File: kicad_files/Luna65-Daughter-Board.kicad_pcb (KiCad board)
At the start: 2 copper layers, 25.1 x 25.1 mm, 38 parts, among them J1 TYPE-C-31-M12, J2 Molex Power, J3 JSTPH, Q1 MMUN2133LT1G, U1 MCP73831, U2 USBLC6-2SC6, U3 AP2112, U4 APX803L, U5 TPS61032RSAR

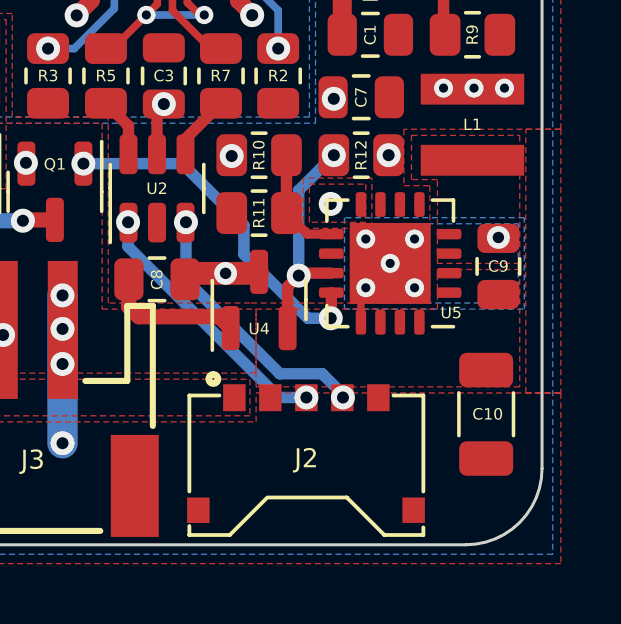
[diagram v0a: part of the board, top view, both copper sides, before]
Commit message: Limit RGB max brightness
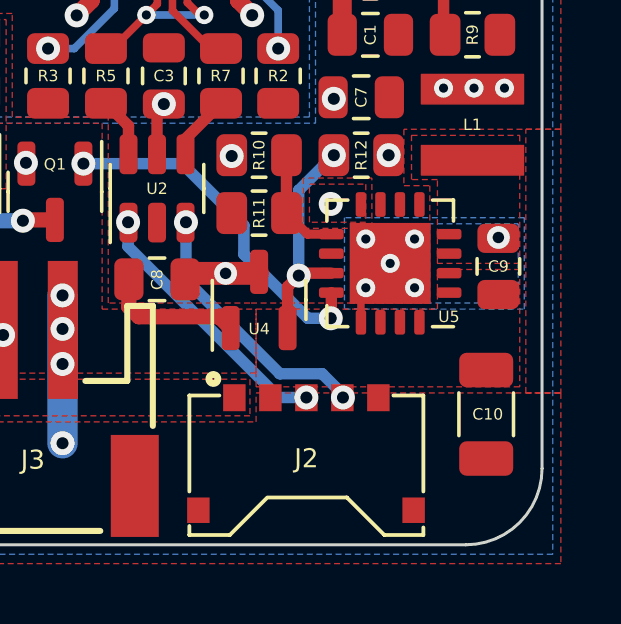
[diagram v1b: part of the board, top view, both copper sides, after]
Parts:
- R4: value 1K -> 2K
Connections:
- J3 pad NC1: GND -> (no net)
- J3 pad NC2: GND -> (no net)
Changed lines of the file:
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@@
       (effects (font (size 0.381 0.381) (thickness 0.0762)))
     )
-    (fp_text value "1K" (at 0 1.65) (layer "F.Fab")
+    (fp_text value "2K" (at 0 1.65) (layer "F.Fab")
       (effects (font (size 1 1) (thickness 0.15)))
     )
@@
       (net 22 "VBAT") (pinfunction "Pin_2") (pintype "passive") (solder_mask_margin 0.0508))
     (pad "NC1" smd rect (at -3.399993 -1.499997 270) (size 3.400001 1.6) (layers "F.Cu" "F.Paste" "F.Mask")
-      (net 1 "GND") (solder_mask_margin 0.0508))
+      (solder_mask_margin 0.0508))
     (pad "NC2" smd rect (at 3.399993 -1.499997 270) (size 3.400001 1.6) (layers "F.Cu" "F.Paste" "F.Mask")
-      (net 1 "GND") (solder_mask_margin 0.0508))
+      (solder_mask_margin 0.0508))
     (model "${KIPRJMOD}/libraries/S2B-PH-SM4-TB.STEP"
       (offset (xyz 0 3.175 0))
@@
     (property "Sheetname" "")
     (attr smd)
-    (fp_text reference "U5" (at -2.032 -1.651 180) (layer "F.SilkS")
+    (fp_text reference "U5" (at -1.9558 -1.778 180) (layer "F.SilkS")
       (effects (font (size 0.381 0.381) (thickness 0.0762)))
     )
@@
       (effects (font (size 1 1) (thickness 0.15)))
     )
+    (fp_line (start -1.41 2.11) (end -2.11 2.11) (layer "F.SilkS") (width 0.12))
+    (fp_line (start -2.11 2.11) (end -2.11 1.41) (layer "F.SilkS") (width 0.12))
+    (fp_line (start 1.41 2.11) (end 2.11 2.11) (layer "F.SilkS") (width 0.12))
+    (fp_line (start -1.41 -2.11) (end -2.11 -2.11) (layer "F.SilkS") (width 0.12))
     (fp_line (start 1.41 -2.11) (end 2.11 -2.11) (layer "F.SilkS") (width 0.12))
+    (fp_line (start 2.11 2.11) (end 2.11 1.41) (layer "F.SilkS") (width 0.12))
     (fp_line (start 2.11 -2.11) (end 2.11 -1.41) (layer "F.SilkS") (width 0.12))
-    (fp_line (start 2.11 2.11) (end 2.11 1.41) (layer "F.SilkS") (width 0.12))
-    (fp_line (start 1.41 2.11) (end 2.11 2.11) (layer "F.SilkS") (width 0.12))
-    (fp_line (start -2.11 2.11) (end -2.11 1.41) (layer "F.SilkS") (width 0.12))
-    (fp_line (start -1.41 -2.11) (end -2.11 -2.11) (layer "F.SilkS") (width 0.12))
-    (fp_line (start -1.41 2.11) (end -2.11 2.11) (layer "F.SilkS") (width 0.12))
+    (fp_line (start -2.62 -2.62) (end -2.62 2.62) (layer "F.CrtYd") (width 0.05))
     (fp_line (start 2.62 2.62) (end 2.62 -2.62) (layer "F.CrtYd") (width 0.05))
+    (fp_line (start 2.62 -2.62) (end -2.62 -2.62) (layer "F.CrtYd") (width 0.05))
     (fp_line (start -2.62 2.62) (end 2.62 2.62) (layer "F.CrtYd") (width 0.05))
-    (fp_line (start 2.62 -2.62) (end -2.62 -2.62) (layer "F.CrtYd") (width 0.05))
-    (fp_line (start -2.62 -2.62) (end -2.62 2.62) (layer "F.CrtYd") (width 0.05))
+    (fp_line (start 2 -2) (end 2 2) (layer "F.Fab") (width 0.1))
     (fp_line (start -2 -1) (end -1 -2) (layer "F.Fab") (width 0.1))
     (fp_line (start 2 2) (end -2 2) (layer "F.Fab") (width 0.1))
+    (fp_line (start -2 2) (end -2 -1) (layer "F.Fab") (width 0.1))
     (fp_line (start -1 -2) (end 2 -2) (layer "F.Fab") (width 0.1))
-    (fp_line (start -2 2) (end -2 -1) (layer "F.Fab") (width 0.1))
-    (fp_line (start 2 -2) (end 2 2) (layer "F.Fab") (width 0.1))
+    (pad "" smd roundrect (at -0.9 -0.9 180) (size 0.73 0.73) (layers "F.Paste") (roundrect_rratio 0.25))
     (pad "" smd roundrect (at 0 -0.9 180) (size 0.73 0.73) (layers "F.Paste") (roundrect_rratio 0.25))
-    (pad "" smd roundrect (at 0 0 180) (size 0.73 0.73) (layers "F.Paste") (roundrect_rratio 0.25))
     (pad "" smd roundrect (at 0.9 -0.9 180) (size 0.73 0.73) (layers "F.Paste") (roundrect_rratio 0.25))
-    (pad "" smd roundrect (at 0 0.9 180) (size 0.73 0.73) (layers "F.Paste") (roundrect_rratio 0.25))
     (pad "" smd roundrect (at 0.9 0 180) (size 0.73 0.73) (layers "F.Paste") (roundrect_rratio 0.25))
+    (pad "" smd roundrect (at 0.9 0.9 180) (size 0.73 0.73) (layers "F.Paste") (roundrect_rratio 0.25))
     (pad "" smd roundrect (at -0.9 0.9 180) (size 0.73 0.73) (layers "F.Paste") (roundrect_rratio 0.25))
     (pad "" smd roundrect (at -0.9 0 180) (size 0.73 0.73) (layers "F.Paste") (roundrect_rratio 0.25))
-    (pad "" smd roundrect (at -0.9 -0.9 180) (size 0.73 0.73) (layers "F.Paste") (roundrect_rratio 0.25))
-    (pad "" smd roundrect (at 0.9 0.9 180) (size 0.73 0.73) (layers "F.Paste") (roundrect_rratio 0.25))
+    (pad "" smd roundrect (at 0 0.9 180) (size 0.73 0.73) (layers "F.Paste") (roundrect_rratio 0.25))
+    (pad "" smd roundrect (at 0 0 180) (size 0.73 0.73) (layers "F.Paste") (roundrect_rratio 0.25))
     (pad "1" smd roundrect (at -1.9625 -0.975 180) (size 0.825 0.35) (layers "F.Cu" "F.Paste" "F.Mask") (roundrect_rratio 0.25)
       (net 23 "5V") (pinfunction "VOUT") (pintype "output"))
@@
     (pad "17" smd rect (at 0 0 180) (size 2.7 2.7) (layers "F.Cu" "F.Mask")
       (net 1 "GND") (pinfunction "GND") (pintype "power_in"))
-    (model "${KICAD6_3DMODEL_DIR}/Package_DFN_QFN.3dshapes/Texas_S-PVQFN-N16_EP2.7x2.7mm.step"
-      (offset (xyz 0 0 0))
-      (scale (xyz 1 1 1))
+    (model "${KICAD6_3DMODEL_DIR}/Package_DFN_QFN.3dshapes/Texas_S-PVQFN-N16_EP2.7x2.7mm.wrl"
+      (offset (xyz 0 0 0))
+      (scale (xyz 1 1 1))

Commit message: DB Rev 4 Changes
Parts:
- removed U1: MCP73831, Package_TO_SOT_SMD:SOT-23-5
- added R14: 1K, Resistor_SMD:R_0805_2012Metric, F.Cu at (92.3, 62.5)
- added U6: LTC4095, Package_DFN_QFN:DFN-8-1EP_2x2mm_P0.5mm_EP0.7x1.3mm, F.Cu at (92.3, 58.3)
- C2: value 10uF -> 1uF
- Q1: value MMUN2133LT1G -> TP0610T
- R4: value 2K -> 1K
- R6: value 1K -> 842
- moved R6 3.56 mm to (95.9, 55.9), turned to 0 degrees
- moved R4 3.54 mm to (92.4, 55.9)
- moved C2 1.63 mm to (92.3, 60.5)
- moved C6 0.48 mm to (92.3, 64.6)
- moved R13 0.48 mm to (92.3, 66.5)
- moved D3 0.20 mm to (109.3, 52.4)
- moved D1 0.18 mm to (96.3, 52.5)
- moved C4 0.18 mm to (95.9, 57.8)
- moved R8 0.18 mm to (95.9, 59.7)
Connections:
- C2 pad 1: GND -> VUSB
- C2 pad 2: VBAT -> GND
- Q1 pad 2: VBAT -> 5V
- R4 pad 2: GND -> Net-(D1-Pad1)
- R6 pad 2: Net-(D1-Pad1) -> GND
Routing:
- net /LBO: track 11.8 -> 19.2 mm, vias 2 -> 3
- net 5V: track 0.00 -> 6.49 mm, vias 0 -> 2
- net GND: track 15.1 -> 17.4 mm, vias 10 -> 11
- net Net-(D1-Pad1): track 5.68 -> 3.72 mm, vias 2 -> 0
- net VUSB: track 4.45 -> 6.35 mm, vias 5 -> 6
- net D+: track 8.84 -> 10.6 mm
- net D-: track 8.84 -> 10.3 mm
- net Net-(R4-Pad1): track 4.84 -> 3.39 mm
- net Net-(R6-Pad1): track 1.82 -> 2.96 mm
- net Net-(D2-Pad2): track 3.52 -> 2.94 mm
- net VBAT: track 2.50 -> 2.91 mm, vias 11 -> 10

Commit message: V7 Changes
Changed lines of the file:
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@@
   (segment (start 105.791 57.3532) (end 105.772794 57.3532) (width 0.5588) (layer "F.Cu") (net 4))
   (segment (start 105.772794 57.3532) (end 105.251141 56.831547) (width 0.5588) (layer "F.Cu") (net 4))
+  (segment (start 93.2915 57.0394) (end 93.2915 57.543) (width 0.3048) (layer "F.Cu") (net 4))
   (segment (start 100.351141 56.898864) (end 100.351141 56.084437) (width 0.5588) (layer "F.Cu") (net 4))
+  (segment (start 93.2942 57.0367) (end 93.2915 57.0394) (width 0.3048) (layer "F.Cu") (net 4))
   (segment (start 93.2661 59.043) (end 93.2661 60.5278) (width 0.381) (layer "F.Cu") (net 4))
   (segment (start 99.861364 57.388641) (end 100.351141 56.898864) (width 0.5588) (layer "F.Cu") (net 4))
-  (segment (start 93.2942 57.1319) (end 93.2915 57.1346) (width 0.3048) (layer "F.Cu") (net 4))
   (segment (start 102.5398 62.0245) (end 102.5398 60.5767) (width 0.381) (layer "F.Cu") (net 4))
-  (segment (start 93.2915 57.1346) (end 93.2915 57.543) (width 0.3048) (layer "F.Cu") (net 4))
   (via (at 96.2914 50.9778) (size 0.8) (drill 0.4) (layers "F.Cu" "B.Cu") (net 4))
-  (via (at 93.2942 57.13189) (size 0.762) (drill 0.381) (layers "F.Cu" "B.Cu") (net 4))
+  (via (at 93.2942 57.0367) (size 0.6096) (drill 0.3048) (layers "F.Cu" "B.Cu") (net 4))
   (via (at 93.266108 60.527794) (size 0.762) (drill 0.381) (layers "F.Cu" "B.Cu") (net 4))
   (via (at 99.7712 57.3532) (size 0.762) (drill 0.381) (layers "F.Cu" "B.Cu") (net 4))
@@
   (segment (start 102.8446 64.9478) (end 103.505 64.2874) (width 0.381) (layer "B.Cu") (net 18))
   (segment (start 104.9274 65.9915) (end 105.8926 65.9915) (width 0.762) (layer "F.Cu") (net 20))
+  (segment (start 91.3665 57.0394) (end 91.3665 57.543) (width 0.3048) (layer "F.Cu") (net 20))
+  (segment (start 91.3638 57.0367) (end 91.3665 57.0394) (width 0.3048) (layer "F.Cu") (net 20))
   (segment (start 103.6759 65.9915) (end 103.4773 66.1901) (width 0.762) (layer "F.Cu") (net 20))
   (segment (start 104.9274 65.9915) (end 103.6759 65.9915) (width 0.762) (layer "F.Cu") (net 20))
-  (segment (start 91.3638 57.1319) (end 91.3665 57.1346) (width 0.3048) (layer "F.Cu") (net 20))
-  (segment (start 91.3665 57.1346) (end 91.3665 57.543) (width 0.3048) (layer "F.Cu") (net 20))
-  (via (at 91.3638 57.13189) (size 0.762) (drill 0.381) (layers "F.Cu" "B.Cu") (net 20))
+  (via (at 91.3638 57.0367) (size 0.6096) (drill 0.3048) (layers "F.Cu" "B.Cu") (net 20))
   (via (at 112.0902 59.817) (size 0.635) (drill 0.3048) (layers "F.Cu" "B.Cu") (net 20))
   (via (at 110.2614 62.0522) (size 0.6096) (drill 0.3048) (layers "F.Cu" "B.Cu") (net 20))

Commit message: stuff
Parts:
- removed U6: LTC4095, Package_DFN_QFN:DFN-8-1EP_2x2mm_P0.5mm_EP0.7x1.3mm
- added C11: 10uF, Capacitor_SMD:C_0603_1608Metric, F.Cu at (92.0, 54.1)
- added C12: 10uF, Capacitor_SMD:C_0603_1608Metric, F.Cu at (94.3, 61.6)
- added L2: 1.5uH, Inductor_SMD:L_0805_2012Metric, F.Cu at (96.7, 56.6)
- added U1: LTC4001, Package_DFN_QFN:QFN-16-1EP_4x4mm_P0.65mm_EP2.15x2.15mm, F.Cu at (93.1, 57.5)
- C1, C3, C4, C5, C6, C7, C8, C9: footprint acheron_Components:C_0805_2012Metric -> Capacitor_SMD:C_0603_1608Metric
- C2: value 1uF -> 0.1uF; footprint acheron_Components:C_0805_2012Metric -> Capacitor_SMD:C_0603_1608Metric
- D1, D2: footprint LED_SMD:LED_1206_3216Metric_Pad1.42x1.75mm_HandSolder -> LED_SMD:LED_0805_2012Metric
- R1, R10, R11, R12, R13, R14, R2, R3, R4, R5, R7, R8, R9: footprint Resistor_SMD:R_0805_2012Metric -> Resistor_SMD:R_0603_1608Metric
- R6: value 842 -> 274; footprint Resistor_SMD:R_0805_2012Metric -> Resistor_SMD:R_0603_1608Metric
- moved C8 9.72 mm to (109.2, 59.1), turned to 90 degrees
- moved C4 8.60 mm to (102.0, 63.9), turned to 0 degrees
- moved Q1 7.53 mm to (92.3, 66.3), turned to 180 degrees
- moved R6 7.39 mm to (91.2, 61.6), turned to 90 degrees
- moved U4 5.76 mm to (105.2, 61.2)
- moved R12 4.77 mm to (105.0, 63.9), turned to 0 degrees
- moved C6 4.56 mm to (95.8, 61.6), turned to 90 degrees
- moved R8 3.51 mm to (98.6, 57.5), turned to -90 degrees
- moved U3 3.32 mm to (98.3, 61.1)
- moved R4 3.21 mm to (95.0, 54.1)
- moved C1 3.20 mm to (110.8, 55.1), turned to 90 degrees
- moved C7 3.14 mm to (107.7, 57.5), turned to 90 degrees
- moved R9 3.06 mm to (112.3, 55.1), turned to 90 degrees
- moved R14 3.06 mm to (95.0, 63.9)
- moved R13 2.66 mm to (92.0, 63.9), turned to 0 degrees
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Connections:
- C2 pad 1: VUSB -> Net-(C2-Pad1)
- R6 pad 1: Net-(R6-Pad1) -> GND
- R6 pad 2: GND -> Net-(R6-Pad2)
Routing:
- net GND: track 17.4 -> 10.1 mm, vias 11 -> 15
- net 5V: track 6.49 -> 1.97 mm, vias 2 -> 3
- net Net-(Q1-Pad3): track 6.83 -> 2.35 mm, vias 2 -> 0
- net /LBO: track 19.2 -> 23.3 mm, vias 3 -> 2
- net Net-(J1-PadB5): track 6.46 -> 2.56 mm, vias 2 -> 0
- net Net-(J1-PadA5): track 6.54 -> 3.53 mm, vias 2 -> 0
- net VBAT: track 3.00 -> 0.00 mm, vias 10 -> 12
- net Net-(R6-Pad1): track 2.96 -> 0.00 mm
- net Net-(D2-Pad2): track 2.94 -> 5.72 mm, vias 0 -> 2
- net Net-(L2-Pad1): track 0.00 -> 2.45 mm
- net /EN: track 7.52 -> 5.46 mm, vias 2 -> 0
- net D-: track 10.3 -> 12.3 mm
- net D+: track 10.6 -> 12.3 mm
- net Net-(L2-Pad2): track 0.00 -> 1.55 mm
- net Net-(C2-Pad1): track 0.00 -> 1.49 mm
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- added copper zone on B.Cu, net 5V
- added copper zone on F.Cu, net Net-(R6-Pad2)
- added copper zone on F.Cu, net VUSB
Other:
- board size 25.1 x 25.1 mm -> 25.4 x 25.4 mm

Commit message: DB Rev 8
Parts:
- removed L2: 1.5uH, Inductor_SMD:L_0805_2012Metric
- added R15: 10K, Resistor_SMD:R_0603_1608Metric, F.Cu at (92.8, 62.0)
- added R16: 1K, Resistor_SMD:R_0603_1608Metric, F.Cu at (95.0, 53.9)
- added R17: 1.5K, Resistor_SMD:R_0603_1608Metric, F.Cu at (92.8, 54.7)
- C11, C12: value 10uF -> 4.7uF
- C2: value 0.1uF -> 1uF
- D1: value Green -> Orange
- R10: value 2.34M -> 2.43M
- R4: value 1K -> 8K
- R6: value 274 -> 10K
- U1: value LTC4001 -> BQ24074RGT; footprint Package_DFN_QFN:QFN-16-1EP_4x4mm_P0.65mm_EP2.15x2.15mm -> Package_DFN_QFN:VQFN-16-1EP_3x3mm_P0.5mm_EP1.6x1.6mm
- U4: value APX803L -> APX803L-35
- moved R4 8.77 mm to (91.3, 62.0), turned to 90 degrees
- moved C11 8.28 mm to (94.3, 62.0), turned to 90 degrees
- moved C4 7.43 mm to (98.2, 57.5), turned to 90 degrees
- moved C6 6.96 mm to (102.4, 63.9), turned to 0 degrees
- moved C12 6.24 mm to (95.0, 55.4), turned to 180 degrees
- moved C2 5.87 mm to (91.3, 55.9)
- moved R8 5.31 mm to (95.8, 62.0)
- moved R6 2.64 mm to (91.3, 59.0), turned to -90 degrees
- moved U1 1.36 mm to (94.2, 58.3), turned to 90 degrees
- moved R11 0.94 mm to (107.7, 64.4)
- moved R10 0.90 mm to (107.7, 61.4)
- moved C7 0.89 mm to (107.7, 58.3)
- moved C8 0.79 mm to (109.2, 58.3)
- moved R12 0.46 mm to (105.4, 63.9)
- moved R2 0.43 mm to (105.7, 57.5)
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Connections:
- C11 pad 1: VUSB -> GND
- C11 pad 2: GND -> +BATT
- C12 pad 1: VBAT -> GND
- C12 pad 2: GND -> VCC
- C2 pad 1: Net-(C2-Pad1) -> GND
- C2 pad 2: GND -> VBUS
- C3 pad 2: VUSB -> VBUS
- C4 pad 1: 5V -> VCC
- C7 pad 1: VBAT -> VCC
- C8 pad 1: VBAT -> VCC
- D1 pad 2: VUSB -> Net-(D1-Pad2)
- J1 pad A4: VUSB -> VBUS
- J1 pad B4: VUSB -> VBUS
- J3 pad 2: VBAT -> +BATT
- L1 pad 1: VBAT -> VCC
- R10 pad 1: VBAT -> VCC
- R12 pad 1: VBAT -> VCC
- R4 pad 1: Net-(R4-Pad1) -> GND
- R4 pad 2: Net-(D1-Pad1) -> Net-(R4-Pad2)
- R8 pad 1: 5V -> VCC
- U1 pad 1: VBAT -> Net-(R15-Pad1)
- U1 pad 10: unconnected-(U1-Pad10) -> VCC
- U1 pad 11: GND -> VCC
- U1 pad 12: Net-(R6-Pad2) -> Net-(R17-Pad2)
- U1 pad 13: Net-(R6-Pad2) -> VBUS
- U1 pad 14: Net-(C2-Pad1) -> GND
- U1 pad 15: GND -> Net-(R6-Pad2)
- U1 pad 16: VBAT -> Net-(R4-Pad2)
- U1 pad 2: Net-(L2-Pad2) -> +BATT
- U1 pad 3: GND -> +BATT
- U1 pad 5: Net-(L2-Pad1) -> VCC
- U1 pad 7: Net-(R4-Pad1) -> unconnected-(U1-Pad7)
- U1 pad 8: VUSB -> GND
- U1 pad 9: VUSB -> Net-(D1-Pad1)
- U2 pad 5: VUSB -> VBUS
- U3 pad 1: 5V -> VCC
- U4 pad 3: VBAT -> VCC
- U5 pad 8: VBAT -> VCC
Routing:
- net 5V: track 1.97 -> 17.8 mm, vias 3 -> 2
- net GND: track 10.1 -> 1.69 mm, vias 15 -> 0
- net VCC: track 0.00 -> 8.17 mm, vias 0 -> 9
- net VUSB: track 5.82 -> 0.00 mm, vias 5 -> 0
- net /EN: track 5.46 -> 0.00 mm
- net Net-(D1-Pad2): track 0.00 -> 5.05 mm
- net Net-(R8-Pad2): track 0.00 -> 3.54 mm
- net Net-(D1-Pad1): track 2.27 -> 5.68 mm
- net Net-(R4-Pad2): track 0.00 -> 2.69 mm
- net Net-(L2-Pad1): track 2.45 -> 0.00 mm
- net Net-(R6-Pad2): track 0.00 -> 2.35 mm
- net VBUS: track 0.00 -> 2.11 mm, vias 0 -> 4
- net Net-(R4-Pad1): track 2.05 -> 0.00 mm
- net Net-(R17-Pad2): track 0.00 -> 1.66 mm
- net Net-(R15-Pad1): track 0.00 -> 1.65 mm
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- added copper zone on B.Cu, net +BATT
- added copper zone on F.Cu, net +BATT
- added copper zone on F.Cu, net /EN
- added copper zone on F.Cu, net Net-(R10-Pad2)
- added copper zone on B.Cu, net VBUS
- added copper zone on F.Cu, net VBUS
- added copper zone on B.Cu, net VCC
- added copper zone on F.Cu, net VCC
- removed copper zone on B.Cu, net 5V
- removed copper zone on B.Cu, net GND
- removed copper zone on F.Cu, net Net-(R6-Pad2)
- removed copper zone on F.Cu, net Net-(R8-Pad2)
- removed copper zone on B.Cu, net VBAT
- removed copper zone on F.Cu, net VBAT
- removed copper zone on B.Cu, net VUSB
- removed copper zone on F.Cu, net VUSB
